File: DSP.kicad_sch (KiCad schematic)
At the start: 23 parts, among them J2 Conn_01x04, J4 Conn_01x04, J5 Conn_01x04, J7 Conn_01x06, U4 STM32F401RBTx, Y1 16MHz

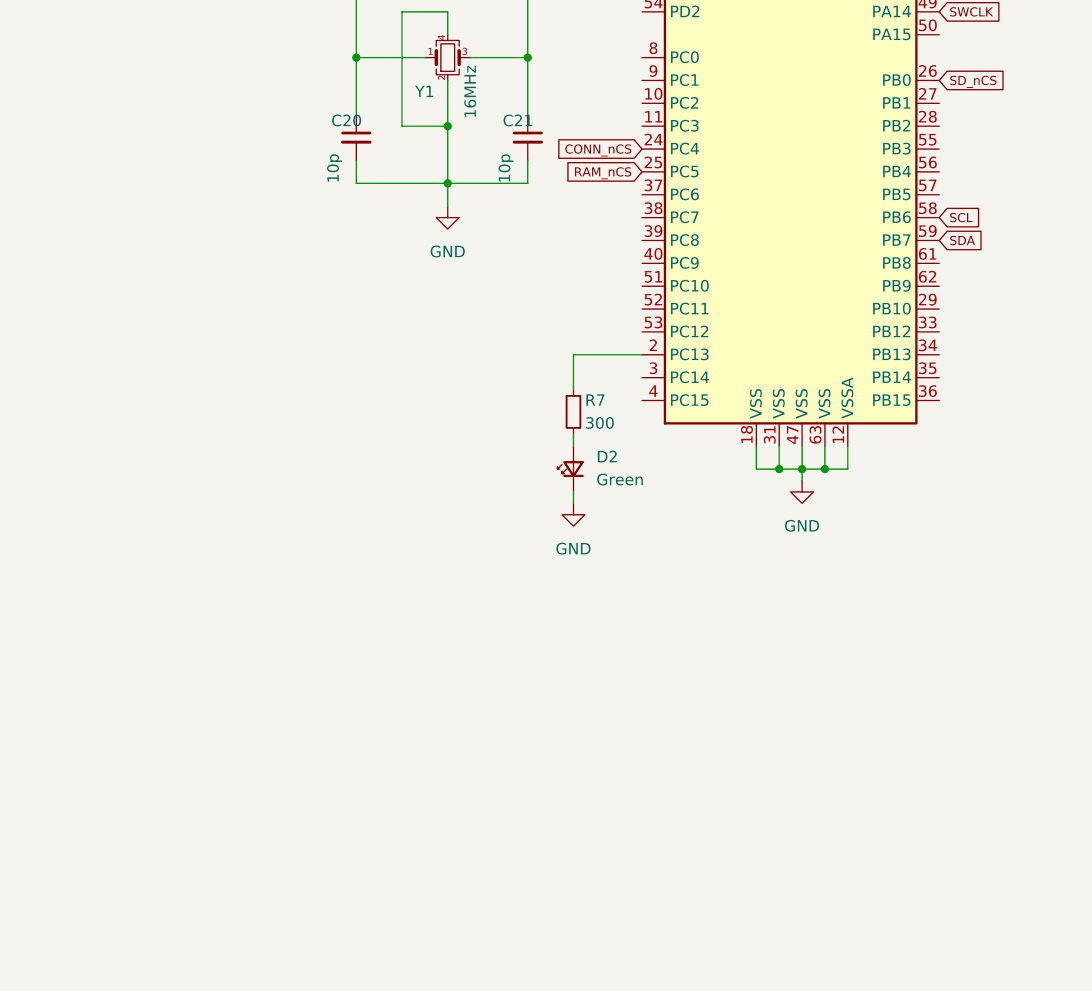
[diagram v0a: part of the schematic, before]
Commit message: smaller pcb removed ram unneccessary
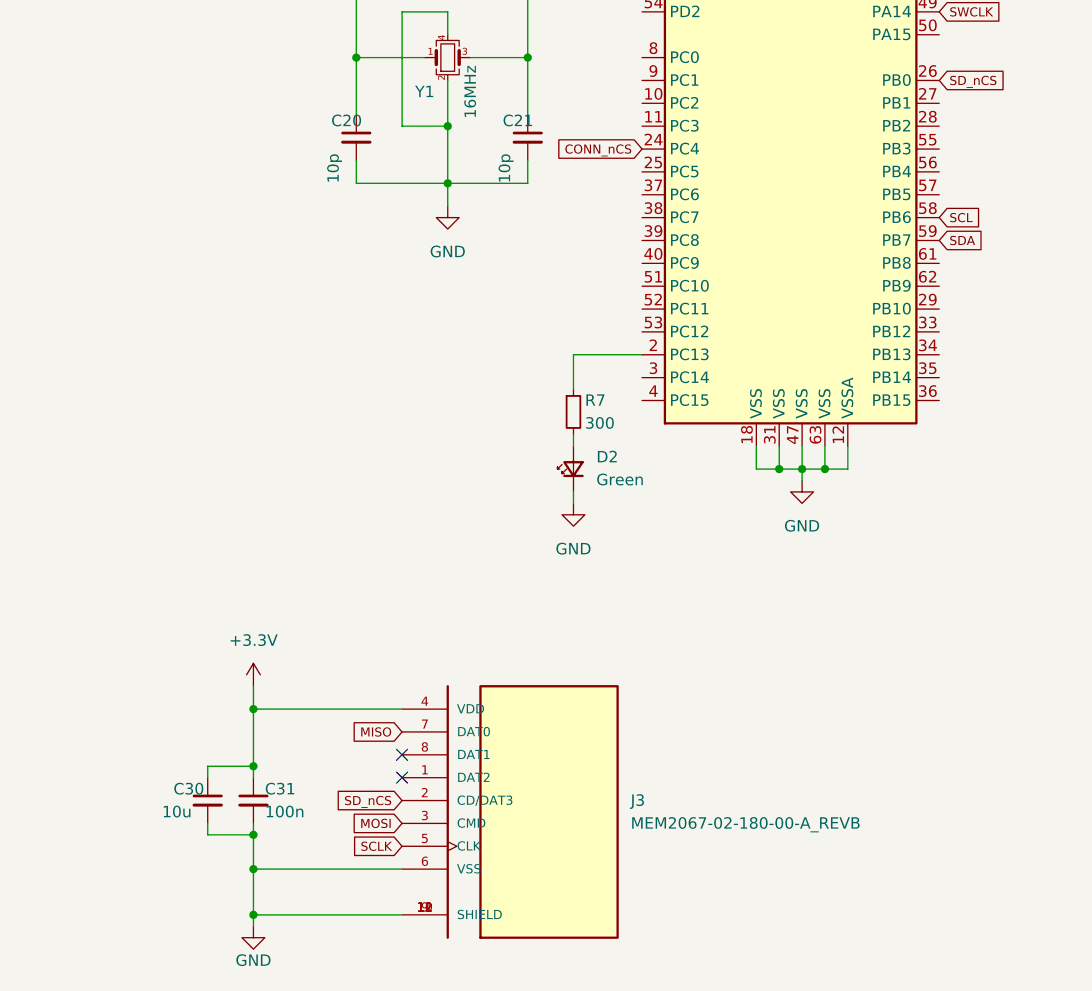
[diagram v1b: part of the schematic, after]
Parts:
- added C30: 10u, Capacitor_SMD:C_0603_1608Metric_Pad1.08x0.95mm_HandSolder, symbol Device:C_Small
- added C31: 100n, Capacitor_SMD:C_0603_1608Metric_Pad1.08x0.95mm_HandSolder, symbol Device:C_Small
- added J3: MEM2067-02-180-00-A_REVB, SnapEda:GCT_MEM2067-02-180-00-A_REVB, symbol MEM2067-02-180-00-A_REVB:MEM2067-02-180-00-A_REVB
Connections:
- net +3V3: now also C30.1, C31.1, J3.4 (VDD)
- net GND: now also C30.2, C31.2, J3.10 (SHIELD), J3.11 (SHIELD), J3.12 (SHIELD), J3.6 (VSS), J3.9 (SHIELD)
- net MISO: now also J3.7 (DAT0)
- net MOSI: now also J3.3 (CMD)
- net SCLK: now also J3.5 (CLK)
- net SD_nCS: now also J3.2 (CD/DAT3)
- net RAM_nCS: no longer names the net of U4.25 (PC5)
- no-connect marks 0 -> 2

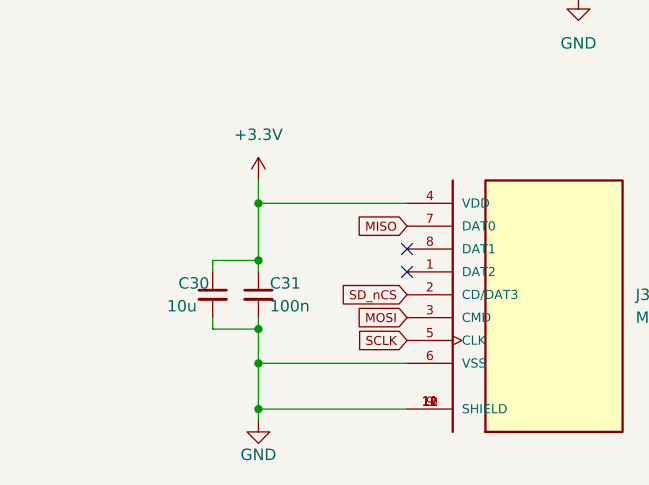
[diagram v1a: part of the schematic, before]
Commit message: smaller mounting holes improved usb routing
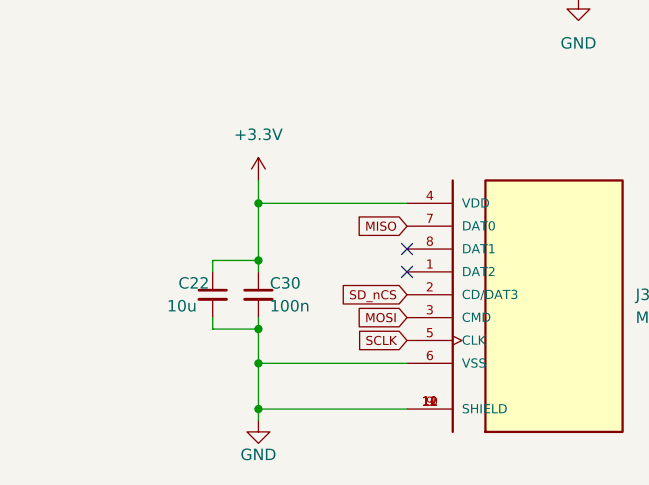
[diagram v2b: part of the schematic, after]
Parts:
- renumbered C30 to C22, C31 to C30
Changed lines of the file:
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@@
   (symbol (lib_id "Device:C_Small") (at 48.26 165.1 0) (unit 1)
     (in_bom yes) (on_board yes) (dnp no)
-    (property "Reference" "C30" (at 44.45 163.83 0)
+    (property "Reference" "C22" (at 44.45 163.83 0)
       (effects (font (size 1.27 1.27)) (justify left))
     )
@@
   (symbol (lib_id "power:GND") (at 53.34 179.07 0) (unit 1)
     (in_bom yes) (on_board yes) (dnp no)
-    (property "Reference" "#PWR0161" (at 53.34 185.42 0)
+    (property "Reference" "#PWR08" (at 53.34 185.42 0)
       (effects (font (size 1.27 1.27)) hide)
     )
@@
   (symbol (lib_id "Device:C_Small") (at 53.34 165.1 0) (unit 1)
     (in_bom yes) (on_board yes) (dnp no)
-    (property "Reference" "C31" (at 54.61 163.83 0)
+    (property "Reference" "C30" (at 54.61 163.83 0)
       (effects (font (size 1.27 1.27)) (justify left))
     )
@@
   (symbol (lib_id "power:+3.3V") (at 53.34 152.4 0) (unit 1)
     (in_bom yes) (on_board yes) (dnp no) (fields_autoplaced)
-    (property "Reference" "#PWR0162" (at 53.34 156.21 0)
-      (effects (font (size 1.27 1.27)) hide)
-    )
+    (property "Reference" "#PWR07" (at 53.34 156.21 0)
+      (effects (font (size 1.27 1.27)) hide)
+    )

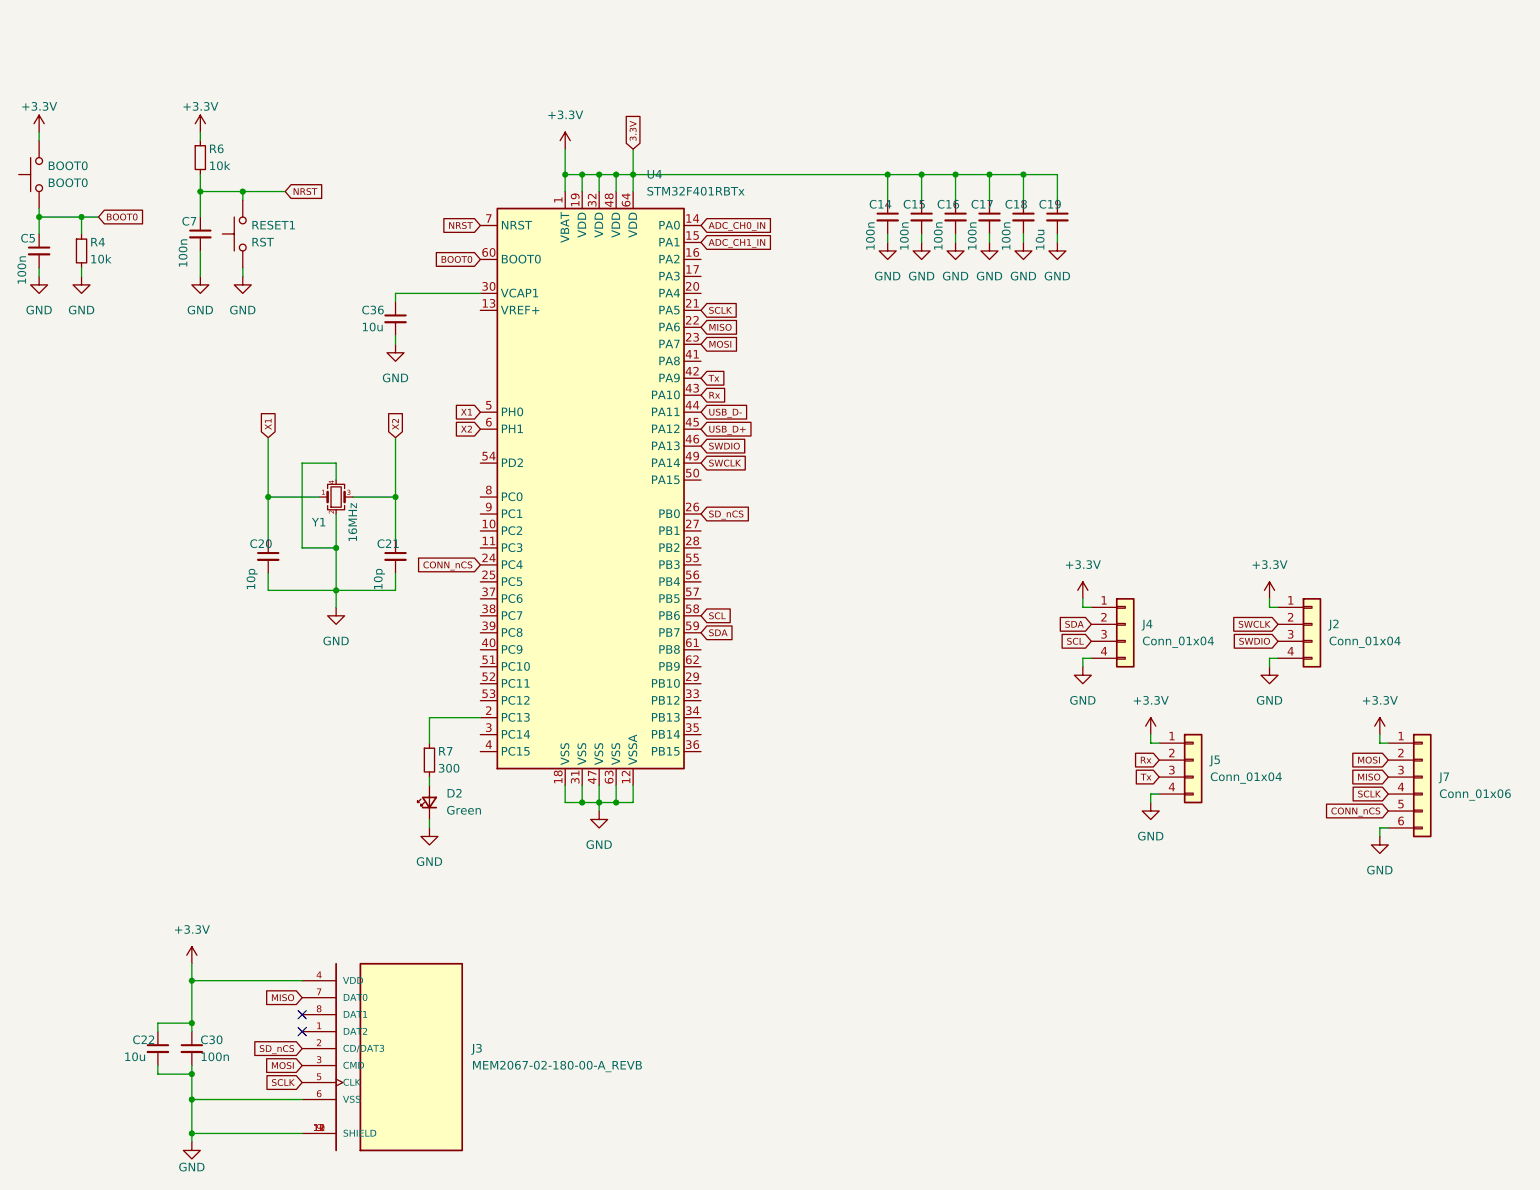
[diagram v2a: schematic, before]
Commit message: moved analog power farther away from digital Power, removed SPI and I2C Interface since it was not needed in the V1
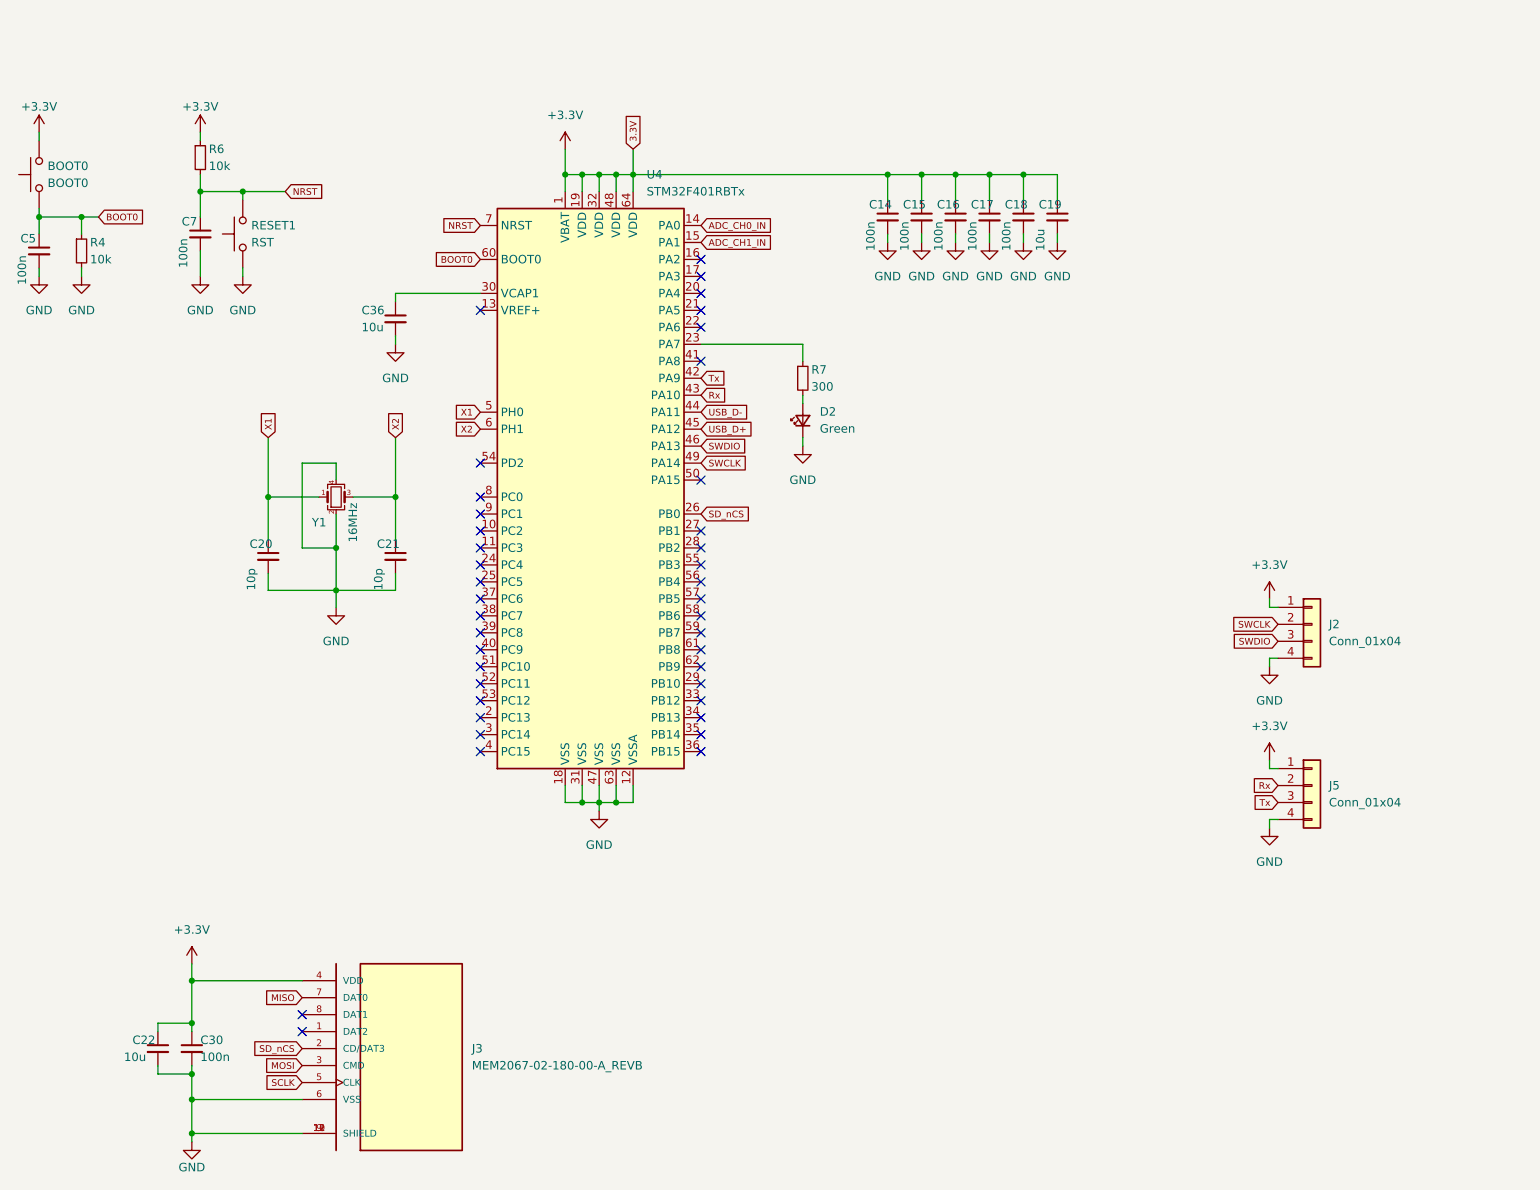
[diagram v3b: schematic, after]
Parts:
- removed J4: Conn_01x04, Connector_PinHeader_2.54mm:PinHeader_1x04_P2.54mm_Vertical, symbol Connector_Generic:Conn_01x04
- removed J7: Conn_01x06, Connector_PinHeader_2.54mm:PinHeader_1x06_P2.54mm_Vertical, symbol Connector_Generic:Conn_01x06
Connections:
- net MISO: no longer U4.22 (PA6)
- net MOSI: no longer U4.23 (PA7)
- net SCLK: no longer U4.21 (PA5)
- net at R7.1: now also U4.23 (PA7); no longer U4.2 (PC13)
- net CONN_nCS: no longer names the net of U4.24 (PC4)
- net SCL: no longer names the net of U4.58 (PB6)
- net SDA: no longer names the net of U4.59 (PB7)
- no-connect marks 2 -> 41
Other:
- moved on the sheet: D2, J5, R7
